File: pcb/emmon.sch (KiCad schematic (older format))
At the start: 37 parts, among them J1 PULSES_CONNECTOR, J2 Conn_01x06, J3 POWER_CONNECTOR, U1 DS3231MZ, U2 AT24CS32-SSHM, U3 ESP-12E, U4 Ai-Thinker-Ra-01, U5 AMS1117-3.3

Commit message: se avanza en el ruteo de pistas
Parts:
- J1: footprint Connector_JST:JST_PH_S3B-PH-K_1x03_P2.00mm_Horizontal -> Connector_JST:JST_PH_B3B-PH-K_1x03_P2.00mm_Vertical
- J2: footprint Connector_JST:JST_PH_S6B-PH-K_1x06_P2.00mm_Horizontal -> Connector_PinHeader_2.54mm:PinHeader_1x06_P2.54mm_Vertical
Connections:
- wire segments 145 -> 148
- no-connect marks 19 -> 18
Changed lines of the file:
@@
-	1    0    0    -1
-$EndComp
-$Comp
-L power:+3.3V #PWR0120
-U 1 1 5ED1131C
-P 5300 2500
-F 0 "#PWR0120" H 5300 2350 50  0001 C CNN
-F 1 "+3.3V" H 5450 2550 50  0000 C CNN
-F 2 "" H 5300 2500 50  0001 C CNN
-F 3 "" H 5300 2500 50  0001 C CNN
-	1    5300 2500
 	1    0    0    -1
 $EndComp
@@
 F 0 "J1" H 1780 3642 50  0000 L CNN
 F 1 "PULSES_CONNECTOR" H 1780 3551 50  0000 L CNN
-F 2 "Connector_JST:JST_PH_S3B-PH-K_1x03_P2.00mm_Horizontal" H 1700 3600 50  0001 C CNN
+F 2 "Connector_JST:JST_PH_B3B-PH-K_1x03_P2.00mm_Vertical" H 1700 3600 50  0001 C CNN
 F 3 "~" H 1700 3600 50  0001 C CNN
 	1    1700 3600
@@
 Wire Notes Line style solid
 	1050 3300 1050 5950
-Wire Notes Line style solid
-	1050 5950 2850 5950
 Wire Notes Line style solid
 	2850 3300 2850 5950
@@
 L power:GND #PWR0136
 U 1 1 5EF90870
-P 2000 5700
-F 0 "#PWR0136" H 2000 5450 50  0001 C CNN
-F 1 "GND" H 2005 5527 50  0000 C CNN
-F 2 "" H 2000 5700 50  0001 C CNN
-F 3 "" H 2000 5700 50  0001 C CNN
-	1    2000 5700
+P 2000 5750
+F 0 "#PWR0136" H 2000 5500 50  0001 C CNN
+F 1 "GND" H 2005 5577 50  0000 C CNN
+F 2 "" H 2000 5750 50  0001 C CNN
+F 3 "" H 2000 5750 50  0001 C CNN
+	1    2000 5750
 	1    0    0    -1
 $EndComp
@@
 	1    0    0    -1
 $EndComp
+Connection ~ 10100 3400
+Wire Wire Line
+	10100 3450 10100 3400
+$Comp
+L power:GND #PWR0107
+U 1 1 5EB7A68C
+P 10100 3450
+F 0 "#PWR0107" H 10100 3200 50  0001 C CNN
+F 1 "GND" H 10105 3277 50  0000 C CNN
+F 2 "" H 10100 3450 50  0001 C CNN
+F 3 "" H 10100 3450 50  0001 C CNN
+	1    10100 3450
+	1    0    0    -1
+$EndComp
+Connection ~ 10100 3100
+Wire Wire Line
+	10100 3050 10100 3100
+$Comp
+L power:+3.3V #PWR0106
+U 1 1 5EB797F1
+P 10100 3050
+F 0 "#PWR0106" H 10100 2900 50  0001 C CNN
+F 1 "+3.3V" H 10250 3100 50  0000 C CNN
+F 2 "" H 10100 3050 50  0001 C CNN
+F 3 "" H 10100 3050 50  0001 C CNN
+	1    10100 3050
+	1    0    0    -1
+$EndComp
+Wire Wire Line
+	10100 3100 10100 3150
+Wire Wire Line
+	10400 3100 10100 3100
+Wire Wire Line
+	10400 3150 10400 3100
+Wire Wire Line
+	10400 3400 10400 3350
+Wire Wire Line
+	10100 3400 10400 3400
+Wire Wire Line
+	10100 3350 10100 3400
+$Comp
+L Device:C_Small C4
+U 1 1 5EB7913C
+P 10400 3250
+F 0 "C4" H 10492 3296 50  0000 L CNN
+F 1 "100n" H 10492 3205 50  0000 L CNN
+F 2 "Resistor_SMD:R_0805_2012Metric" H 10400 3250 50  0001 C CNN
+F 3 "~" H 10400 3250 50  0001 C CNN
+	1    10400 3250
+	1    0    0    -1
+$EndComp
+$Comp
+L Device:C_Small C3
+U 1 1 5EB78F7A
+P 10100 3250
+F 0 "C3" H 10192 3296 50  0000 L CNN
+F 1 "10u" H 10192 3205 50  0000 L CNN
+F 2 "Capacitor_SMD:C_0805_2012Metric" H 10100 3250 50  0001 C CNN
+F 3 "~" H 10100 3250 50  0001 C CNN
+	1    10100 3250
+	1    0    0    -1
+$EndComp
+Wire Wire Line
+	2000 5700 2000 5650
+Wire Wire Line
+	7950 2750 8000 2750
+$Comp
+L Connector_Generic:Conn_01x06 J2
+U 1 1 5F22A1C6
+P 1700 4400
+F 0 "J2" H 1780 4392 50  0000 L CNN
+F 1 "Conn_01x06" H 1780 4301 50  0000 L CNN
+F 2 "Connector_PinHeader_2.54mm:PinHeader_1x06_P2.54mm_Vertical" H 1700 4400 50  0001 C CNN
+F 3 "~" H 1700 4400 50  0001 C CNN
+	1    1700 4400
+	1    0    0    -1
+$EndComp
+Text GLabel 1450 4600 0    50   Input ~ 0
+RST
+Wire Wire Line
+	1450 4600 1500 4600
+Wire Wire Line
+	2500 1950 2500 2000
 $Comp
 L RF_Module:ESP-12E U3
@@
 	1    0    0    -1
 $EndComp
-Connection ~ 10100 3400
-Wire Wire Line
-	10100 3450 10100 3400
-$Comp
-L power:GND #PWR0107
-U 1 1 5EB7A68C
-P 10100 3450
-F 0 "#PWR0107" H 10100 3200 50  0001 C CNN
-F 1 "GND" H 10105 3277 50  0000 C CNN
-F 2 "" H 10100 3450 50  0001 C CNN
-F 3 "" H 10100 3450 50  0001 C CNN
-	1    10100 3450
-	1    0    0    -1
-$EndComp
-Connection ~ 10100 3100
-Wire Wire Line
-	10100 3050 10100 3100
-$Comp
-L power:+3.3V #PWR0106
-U 1 1 5EB797F1
-P 10100 3050
-F 0 "#PWR0106" H 10100 2900 50  0001 C CNN
-F 1 "+3.3V" H 10250 3100 50  0000 C CNN
-F 2 "" H 10100 3050 50  0001 C CNN
-F 3 "" H 10100 3050 50  0001 C CNN
-	1    10100 3050
-	1    0    0    -1
-$EndComp
-Wire Wire Line
-	10100 3100 10100 3150
-Wire Wire Line
-	10400 3100 10100 3100
-Wire Wire Line
-	10400 3150 10400 3100
-Wire Wire Line
-	10400 3400 10400 3350
-Wire Wire Line
-	10100 3400 10400 3400
-Wire Wire Line
-	10100 3350 10100 3400
-$Comp
-L Device:C_Small C4
-U 1 1 5EB7913C
-P 10400 3250
-F 0 "C4" H 10492 3296 50  0000 L CNN
-F 1 "100n" H 10492 3205 50  0000 L CNN
-F 2 "Resistor_SMD:R_0805_2012Metric" H 10400 3250 50  0001 C CNN
-F 3 "~" H 10400 3250 50  0001 C CNN
-	1    10400 3250
-	1    0    0    -1
-$EndComp
-$Comp
-L Device:C_Small C3
-U 1 1 5EB78F7A
-P 10100 3250
-F 0 "C3" H 10192 3296 50  0000 L CNN
-F 1 "10u" H 10192 3205 50  0000 L CNN
-F 2 "Capacitor_SMD:C_0805_2012Metric" H 10100 3250 50  0001 C CNN
-F 3 "~" H 10100 3250 50  0001 C CNN
-	1    10100 3250
-	1    0    0    -1
-$EndComp
-Wire Wire Line
-	2000 5700 2000 5650
-NoConn ~ 1900 5650
-Wire Wire Line
-	7950 2750 8000 2750
-$Comp
-L Connector_Generic:Conn_01x06 J2
-U 1 1 5F22A1C6
-P 1700 4400
-F 0 "J2" H 1780 4392 50  0000 L CNN
-F 1 "Conn_01x06" H 1780 4301 50  0000 L CNN
-F 2 "Connector_JST:JST_PH_S6B-PH-K_1x06_P2.00mm_Horizontal" H 1700 4400 50  0001 C CNN
-F 3 "~" H 1700 4400 50  0001 C CNN
-	1    1700 4400
-	1    0    0    -1
-$EndComp
-Text GLabel 1450 4600 0    50   Input ~ 0
-RST
-Wire Wire Line
-	1450 4600 1500 4600
-Wire Wire Line
-	2500 1950 2500 2000
+$Comp
+L power:+3.3V #PWR0120
+U 1 1 5ED1131C
+P 5300 2500
+F 0 "#PWR0120" H 5300 2350 50  0001 C CNN
+F 1 "+3.3V" H 5450 2550 50  0000 C CNN
+F 2 "" H 5300 2500 50  0001 C CNN
+F 3 "" H 5300 2500 50  0001 C CNN
+	1    5300 2500
+	1    0    0    -1
+$EndComp
+Wire Wire Line
+	1900 5650 1900 5700
+Wire Wire Line
+	1900 5700 2000 5700
+Wire Wire Line
+	2000 5750 2000 5700
+Connection ~ 2000 5700
+Wire Notes Line style solid
+	1050 5950 2850 5950
 $EndSCHEMATC

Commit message: se completa el esquemático y se avanza en el posicionamiento del pcb
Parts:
- removed H1, H2, H3, H4: MountingHole_Pad, MountingHole:MountingHole_3.2mm_M3_Pad_Via, symbol Mechanical:MountingHole_Pad
- removed J1: PULSES_CONNECTOR, Connector_JST:JST_PH_B3B-PH-K_1x03_P2.00mm_Vertical, symbol Connector_Generic:Conn_01x03
- removed J2: Conn_01x06, Connector_PinHeader_2.54mm:PinHeader_1x06_P2.54mm_Vertical, symbol Connector_Generic:Conn_01x06
- removed J3: POWER_CONNECTOR, Connector_USB:USB_Micro-B_Molex_47346-0001, symbol Connector:USB_B_Micro
- removed R4: 12K, Resistor_SMD:R_0805_2012Metric, symbol Device:R_Small
- removed U1: DS3231MZ, Package_SO:SOIC-8_3.9x4.9mm_P1.27mm, symbol Timer_RTC:DS3231MZ
- removed U3: ESP-12E, RF_Module:ESP-12E, symbol RF_Module:ESP-12E
- removed U4: Ai-Thinker-Ra-01, RF_Module:Ai-Thinker-Ra-01-LoRa, symbol RF_Module:Ai-Thinker-Ra-01
- removed U5: AMS1117-3.3, Package_TO_SOT_SMD:SOT-223-3_TabPin2, symbol Regulator_Linear:AMS1117-3.3
- added H1, H2, H3, H4: MountingHole, MountingHole:MountingHole_3.2mm_M3, symbol Mechanical:MountingHole
- added J1: POWER_CONNECTOR, Connector_BarrelJack:BarrelJack_Horizontal, symbol Connector:Barrel_Jack_Switch
- added J2: PROG_CONNECTOR, Connector_PinHeader_2.54mm:PinHeader_2x03_P2.54mm_Horizontal, symbol Connector_Generic:Conn_02x03_Odd_Even
- added J3: SENSOR_CONNECTOR, Connector_PinHeader_2.54mm:PinHeader_1x03_P2.54mm_Horizontal, symbol Connector_Generic:Conn_01x03
- added J4: ANTENNA_CONNECTOR, Connector_Coaxial:SMA_Molex_73251-1153_EdgeMount_Horizontal, symbol Connector:Conn_Coaxial
- added U1: DS3231M, Package_SO:SOIC-16W_7.5x10.3mm_P1.27mm, symbol Timer_RTC:DS3231M
- added U2: AMS1117-3.3, Package_TO_SOT_SMD:SOT-223-3_TabPin2, symbol Regulator_Linear:AMS1117-3.3
- added U3: Ai-Thinker-Ra-01, RF_Module:Ai-Thinker-Ra-01-LoRa, symbol RF_Module:Ai-Thinker-Ra-01
- added U5: ESP-12S, ESP8266:ESP-12S, symbol ESP8266:ESP-12S
- C1: renamed from C10; footprint Capacitor_SMD:C_0805_2012Metric -> Capacitor_SMD:C_0805_2012Metric_Pad1.15x1.40mm_HandSolder
- C10: renamed from C3; value 10u -> 1u; footprint Capacitor_SMD:C_0805_2012Metric -> Capacitor_SMD:C_0805_2012Metric_Pad1.15x1.40mm_HandSolder
- C11: renamed from C4; footprint Resistor_SMD:R_0805_2012Metric -> Capacitor_SMD:C_0805_2012Metric_Pad1.15x1.40mm_HandSolder
- C2: renamed from C6; value 10u -> 1u; footprint Capacitor_SMD:C_0805_2012Metric -> Capacitor_SMD:C_0805_2012Metric_Pad1.15x1.40mm_HandSolder
- C3: renamed from C7; footprint Resistor_SMD:R_0805_2012Metric -> Capacitor_SMD:C_0805_2012Metric_Pad1.15x1.40mm_HandSolder
- C4: renamed from C11; footprint Capacitor_SMD:C_0805_2012Metric -> Capacitor_SMD:C_0805_2012Metric_Pad1.15x1.40mm_HandSolder
- C5: renamed from C8; footprint Capacitor_SMD:C_0805_2012Metric -> Capacitor_SMD:C_0805_2012Metric_Pad1.15x1.40mm_HandSolder
- C6: renamed from C9; footprint Resistor_SMD:R_0805_2012Metric -> Capacitor_SMD:C_0805_2012Metric_Pad1.15x1.40mm_HandSolder
- C7: renamed from C1; value 10u -> 1u; footprint Capacitor_SMD:C_0805_2012Metric -> Capacitor_SMD:C_0805_2012Metric_Pad1.15x1.40mm_HandSolder
- C8: renamed from C2; footprint Capacitor_SMD:C_0805_2012Metric -> Capacitor_SMD:C_0805_2012Metric_Pad1.15x1.40mm_HandSolder
- C9: renamed from C5; value 47p -> 470p; footprint Capacitor_SMD:C_0805_2012Metric -> Capacitor_SMD:C_0805_2012Metric_Pad1.15x1.40mm_HandSolder
- D1: value LED_Small -> LED_POWER; footprint LED_SMD:LED_0805_2012Metric -> LED_THT:LED_D3.0mm
- R1: renamed from R12; footprint Resistor_SMD:R_0805_2012Metric -> Resistor_SMD:R_0805_2012Metric_Pad1.15x1.40mm_HandSolder
- R10: renamed from R9; footprint Resistor_SMD:R_0805_2012Metric -> Resistor_SMD:R_0805_2012Metric_Pad1.15x1.40mm_HandSolder
- R11, R5, R6, R7, R8: footprint Resistor_SMD:R_0805_2012Metric -> Resistor_SMD:R_0805_2012Metric_Pad1.15x1.40mm_HandSolder
- R2: renamed from R1; footprint Resistor_SMD:R_0805_2012Metric -> Resistor_SMD:R_0805_2012Metric_Pad1.15x1.40mm_HandSolder
- R3: renamed from R2; footprint Resistor_SMD:R_0805_2012Metric -> Resistor_SMD:R_0805_2012Metric_Pad1.15x1.40mm_HandSolder
- R4: renamed from R3; footprint Resistor_SMD:R_0805_2012Metric -> Resistor_SMD:R_0805_2012Metric_Pad1.15x1.40mm_HandSolder
- R9: renamed from R10; footprint Resistor_SMD:R_0805_2012Metric -> Resistor_SMD:R_0805_2012Metric_Pad1.15x1.40mm_HandSolder
- renumbered U2 to U4
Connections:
- net labels added: ANT, EN, RX
- net labels removed: DIO0
- wire segments 148 -> 145
- no-connect marks 18 -> 9
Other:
- moved on the sheet: C10, C11, C2, C3, R11, R9

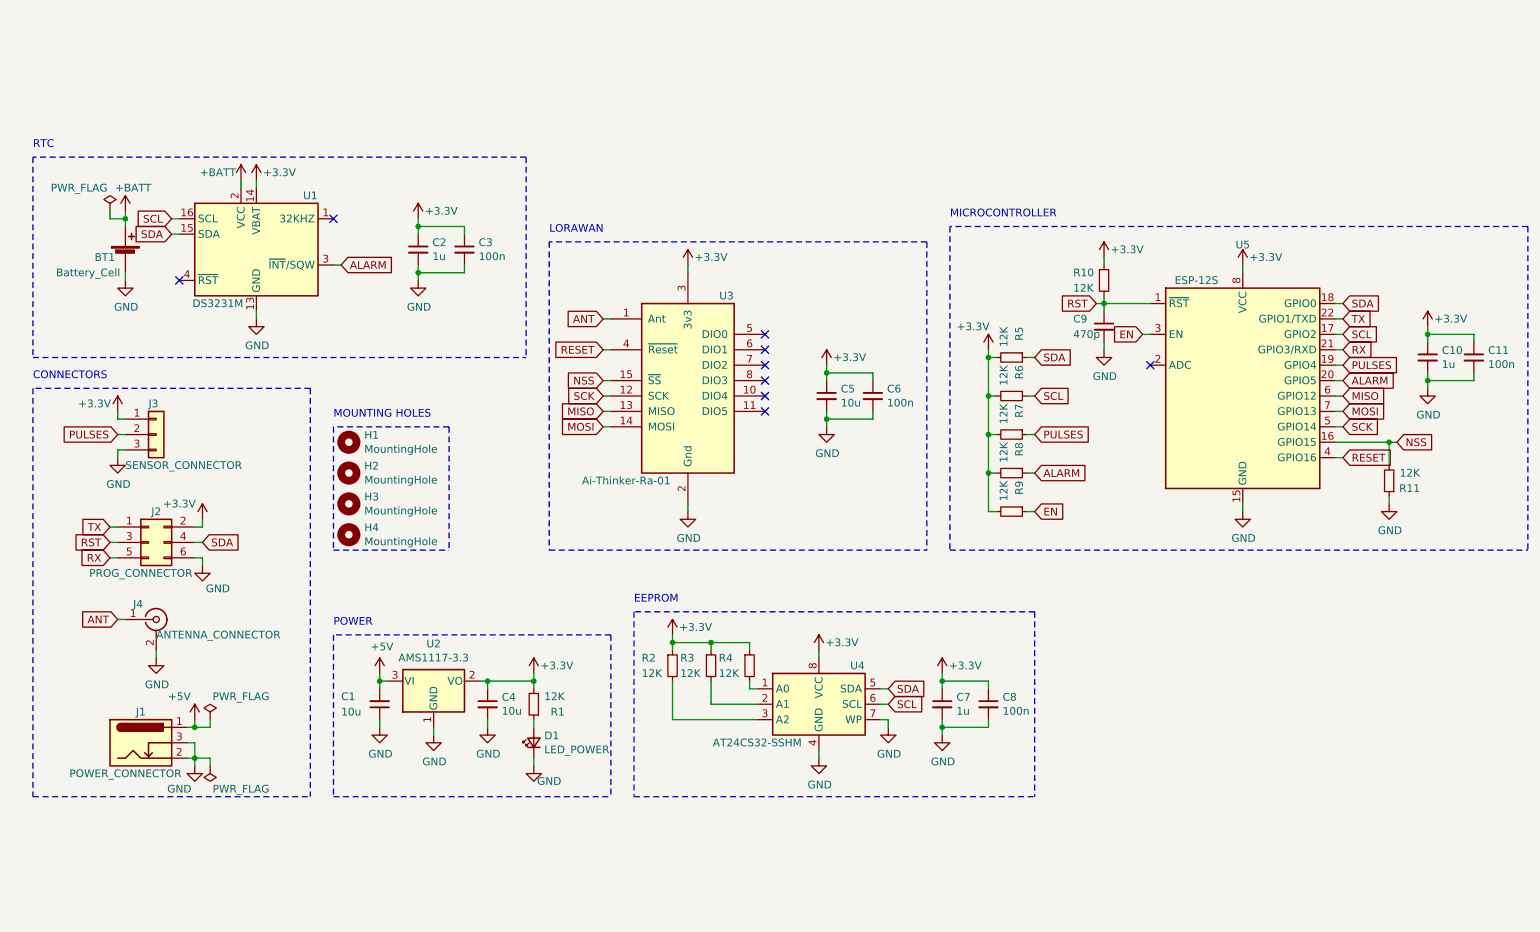
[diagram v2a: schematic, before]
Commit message: se edita el esquemático y se añade el pcb
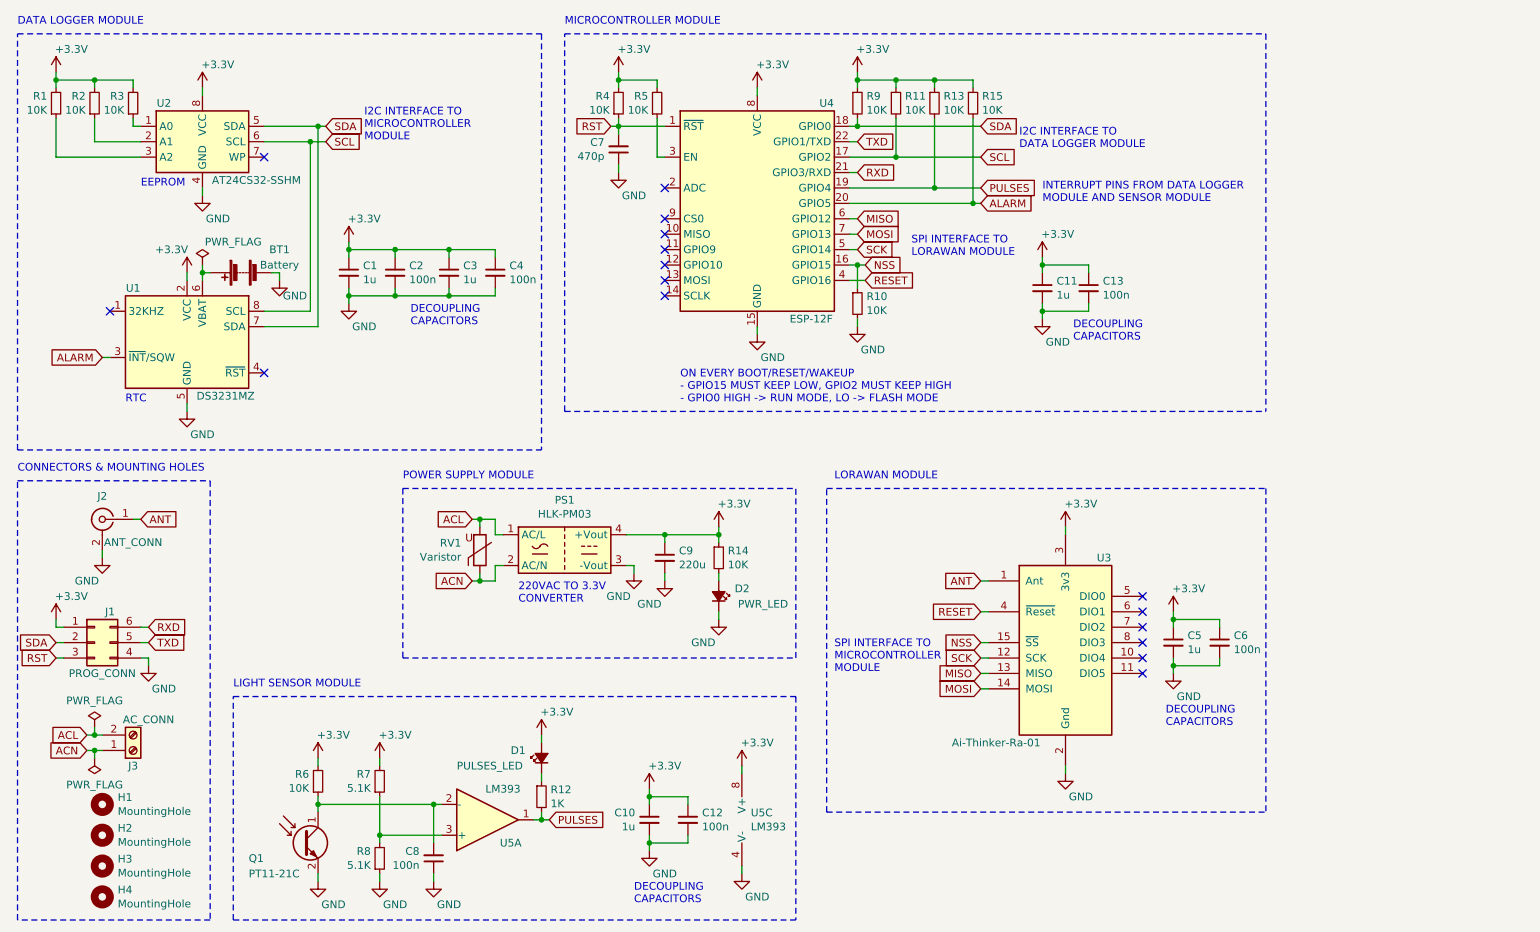
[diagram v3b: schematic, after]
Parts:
- removed BT1: Battery_Cell, Battery:BatteryHolder_Keystone_1060_1x2032, symbol Device:Battery_Cell
- removed D1: LED_POWER, LED_THT:LED_D3.0mm, symbol Device:LED_Small
- removed J1: POWER_CONNECTOR, Connector_BarrelJack:BarrelJack_Horizontal, symbol Connector:Barrel_Jack_Switch
- removed J2: PROG_CONNECTOR, Connector_PinHeader_2.54mm:PinHeader_2x03_P2.54mm_Horizontal, symbol Connector_Generic:Conn_02x03_Odd_Even
- removed J3: SENSOR_CONNECTOR, Connector_PinHeader_2.54mm:PinHeader_1x03_P2.54mm_Horizontal, symbol Connector_Generic:Conn_01x03
- removed J4: ANTENNA_CONNECTOR, Connector_Coaxial:SMA_Molex_73251-1153_EdgeMount_Horizontal, symbol Connector:Conn_Coaxial
- removed U1: DS3231M, Package_SO:SOIC-16W_7.5x10.3mm_P1.27mm, symbol Timer_RTC:DS3231M
- removed U2: AMS1117-3.3, Package_TO_SOT_SMD:SOT-223-3_TabPin2, symbol Regulator_Linear:AMS1117-3.3
- removed U4: AT24CS32-SSHM, Package_SO:SOIC-8_3.9x4.9mm_P1.27mm, symbol Memory_EEPROM:AT24CS32-SSHM
- removed U5: ESP-12S, ESP8266:ESP-12S, symbol ESP8266:ESP-12S
- added BT1: Battery, Battery:BatteryHolder_Keystone_1060_1x2032, symbol Device:Battery
- added C12, C13: 100n, Capacitor_SMD:C_0805_2012Metric_Pad1.15x1.40mm_HandSolder, symbol Device:C_Small
- added D1: PULSES_LED, LED_THT:LED_D3.0mm, symbol Device:LED_Small_ALT
- added D2: PWR_LED, LED_THT:LED_D3.0mm, symbol Device:LED_Small_ALT
- added J1: PROG_CONN, Connector_PinHeader_2.54mm:PinHeader_2x03_P2.54mm_Vertical, symbol Connector_Generic:Conn_02x03_Counter_Clockwise
- added J2: ANT_CONN, Connector_Coaxial:SMA_Molex_73251-1153_EdgeMount_Horizontal, symbol Connector:Conn_Coaxial
- added J3: AC_CONN, TerminalBlock_Phoenix:TerminalBlock_Phoenix_MKDS-1,5-2-5.08_1x02_P5.08mm_Horizontal, symbol Connector:Screw_Terminal_01x02
- added PS1: HLK-PM03, Converter_ACDC:Converter_ACDC_HiLink_HLK-PMxx, symbol Converter_ACDC:HLK-PM03
- added Q1: PT11-21C, LED_SMD:LED_1206_3216Metric_Pad1.42x1.75mm_HandSolder, symbol Device:Q_Photo_NPN
- added R12: 1K, Resistor_SMD:R_0805_2012Metric_Pad1.15x1.40mm_HandSolder, symbol Device:R_Small
- added R13, R14, R15: 10K, Resistor_SMD:R_0805_2012Metric_Pad1.15x1.40mm_HandSolder, symbol Device:R_Small
- added RV1: Varistor, Varistor:RV_Disc_D12mm_W3.9mm_P7.5mm, symbol Device:Varistor
- added U1: DS3231MZ, Package_SO:SOIC-8_3.9x4.9mm_P1.27mm, symbol Timer_RTC:DS3231MZ
- added U2: AT24CS32-SSHM, Package_SO:SOIC-8_3.9x4.9mm_P1.27mm, symbol Memory_EEPROM:AT24CS32-SSHM
- added U4: ESP-12F, RF_Module:ESP-12E, symbol RF_Module:ESP-12F
- added U5: LM393, Package_SO:SOIC-8_3.9x4.9mm_P1.27mm, symbol Comparator:LM393
- C1, C5: value 10u -> 1u
- C11, C3: value 100n -> 1u
- C2: value 1u -> 100n
- C4: value 10u -> 100n
- C7: value 1u -> 470p
- C9: value 470p -> 220u; footprint Capacitor_SMD:C_0805_2012Metric_Pad1.15x1.40mm_HandSolder -> Capacitor_THT:C_Radial_D6.3mm_H11.0mm_P2.50mm
- H1, H2, H3, H4: footprint MountingHole:MountingHole_3.2mm_M3 -> MountingHole:MountingHole_2.7mm_M2.5
- R1, R10, R11, R2, R3, R4, R5, R6, R9: value 12K -> 10K
- R7, R8: value 12K -> 5.1K
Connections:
- net +5V is gone; now on net GND: C1.2
- net EN is gone; now on net +3V3: R9.1
- net +3V3: now also C1.1, C9.1, R11.1, R2.2, R3.2, R4.2, C12.1, C13.1, D1.2 (A), J1.1 (Pin_1), PS1.4 (+Vout), R13.1, R14.1, R15.1, U1.2 (VCC), U2.8 (VCC), U4.8 (VCC), U5.8 (V+); no longer C7.1, C8.1, R10.1, R2.1, R3.1, R4.1, R8.2, R9.2
- net ALARM: now also R15.2, U1.3 (~INT~/SQW), U4.20 (GPIO5); no longer R8.1
- net ANT: now also J2.1 (In)
- net GND: now also C7.1, C8.1, R10.2, R8.1, BT1.2 (-), C12.2, C13.2, D2.1 (K), J1.4 (Pin_4), J2.2 (Ext), PS1.3 (-Vout), Q1.2 (E), U1.5 (GND), U2.4 (GND), U4.15 (GND), U5.4 (V-); no longer C1.1, C7.2, C8.2, R11.1
- net MISO: now also U4.6 (GPIO12)
- net MOSI: now also U4.7 (GPIO13)
- net NSS: now also R10.1, U4.16 (GPIO15); no longer R11.2
- net PULSES: now also R12.2, R13.2, U4.19 (GPIO4), U5.1; no longer R7.1
- net RESET: now also U4.4 (GPIO16)
- net RST: now also C7.2, R4.1, J1.3 (Pin_3), U4.1 (~RST); no longer C9.1, R10.2
- net SCK: now also U4.5 (GPIO14)
- net SCL: now also R11.2, U1.8 (SCL), U2.6 (SCL), U4.17 (GPIO2); no longer R6.1
- net SDA: now also R9.2, J1.2 (Pin_2), U1.7 (SDA), U2.5 (SDA), U4.18 (GPIO0); no longer R5.1
- net at R1.1: now also U2.3 (A2)
- new net: R5.1, U4.3 (EN)
- new net: BT1.1 (+), U1.6 (VBAT)
- new net: R3.1, U2.1 (A0)
- new net: R2.1, U2.2 (A1)
- new net: C8.2, Q1.1 (C), R6.1, U5.2 (-)
- new net: R7.1, R8.2, U5.3 (+)
- new net: D2.2 (A), R14.2
- new net: D1.1 (K), R12.1
- new net ACL: J3.2 (Pin_2), PS1.1 (AC/L), RV1.2
- new net ACN: J3.1 (Pin_1), PS1.2 (AC/N), RV1.1
- new net RXD: J1.6 (Pin_6), U4.21 (GPIO3/RXD)
- new net TXD: J1.5 (Pin_5), U4.22 (GPIO1/TXD)
- no-connect marks 9 -> 16
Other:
- note added: "220VAC TO 3.3V\nCONVERTER"
- note added: "CONNECTORS & MOUNTING HOLES"
- note added: "DATA LOGGER MODULE"
- note added: "DECOUPLING\nCAPACITORS"
- note added: "I2C INTERFACE TO\nDATA LOGGER MODULE"
- note added: "I2C INTERFACE TO\nMICROCONTROLLER\nMODULE"
- note added: "INTERRUPT PINS FROM DATA LOGGER\nMODULE AND SENSOR MODULE"
- note added: "LIGHT SENSOR MODULE"
- note added: "LORAWAN MODULE"
- note added: "MICROCONTROLLER MODULE"
- note added: "ON EVERY BOOT/RESET/WAKEUP\n- GPIO15 MUST KEEP LOW, GPIO2 MUST KEEP HIGH\n- GPIO0 HIGH -> RUN MODE, LO -> FLASH MODE"
- note added: "POWER SUPPLY MODULE"
- note added: "SPI INTERFACE TO \nLORAWAN MODULE"
- note added: "SPI INTERFACE TO \nMICROCONTROLLER\nMODULE"
- note removed: "CONNECTORS"
- note removed: "LORAWAN"
- note removed: "MICROCONTROLLER"
- note removed: "MOUNTING HOLES"
- note removed: "POWER"
